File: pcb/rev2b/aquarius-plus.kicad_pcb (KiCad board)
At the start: 2 copper layers, 167 x 115 mm, 170 parts, among them J1 Power in, J10 FPGA spare, J11 Hand controller 2, J12 Hand controller 1, J13 ESP32 spare, J2 ESP USB Host, J3 Audio out, J4 VGA, J5 Cassette out, J6 Cassette in, J7 Expansion port, J8 Printer, J9 TF-03A, Q1 BC847C, Q2 BC847C, Q3 2N7002, SW1 SW_DPDT_x2, U1 SN74AHCT1G125DBVR, U10 ESP32-S3-WROOM-1-N4R2, U11 LDL1117S33R, U12 SN74CB3T3245PWR, U13 IS61C5128AS-25QLI, U2 SN74AHCT1G125DBVR, U3 LD1117S12, U4 SN74CB3T3245PWR, U5 MAX3221ECPWR, U6 XC6SLX9-2TQG144C, U7 Z84C0010AEG, U8 SN74CB3T3245PWR, U9 SN74CB3T3245PWR, X1 SX3M14.31818M20F30TNN

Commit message: Tweaks
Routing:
- net GND: track 884.0 -> 856.1 mm
- net MREQ#: track 99.7 -> 90.9 mm
- net +3V3: track 540.0 -> 537.5 mm
- net A7: track 135.6 -> 136.8 mm
- net D1: track 108.3 -> 107.7 mm
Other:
- board text added: "rev2b"
- board text removed: "rev2"

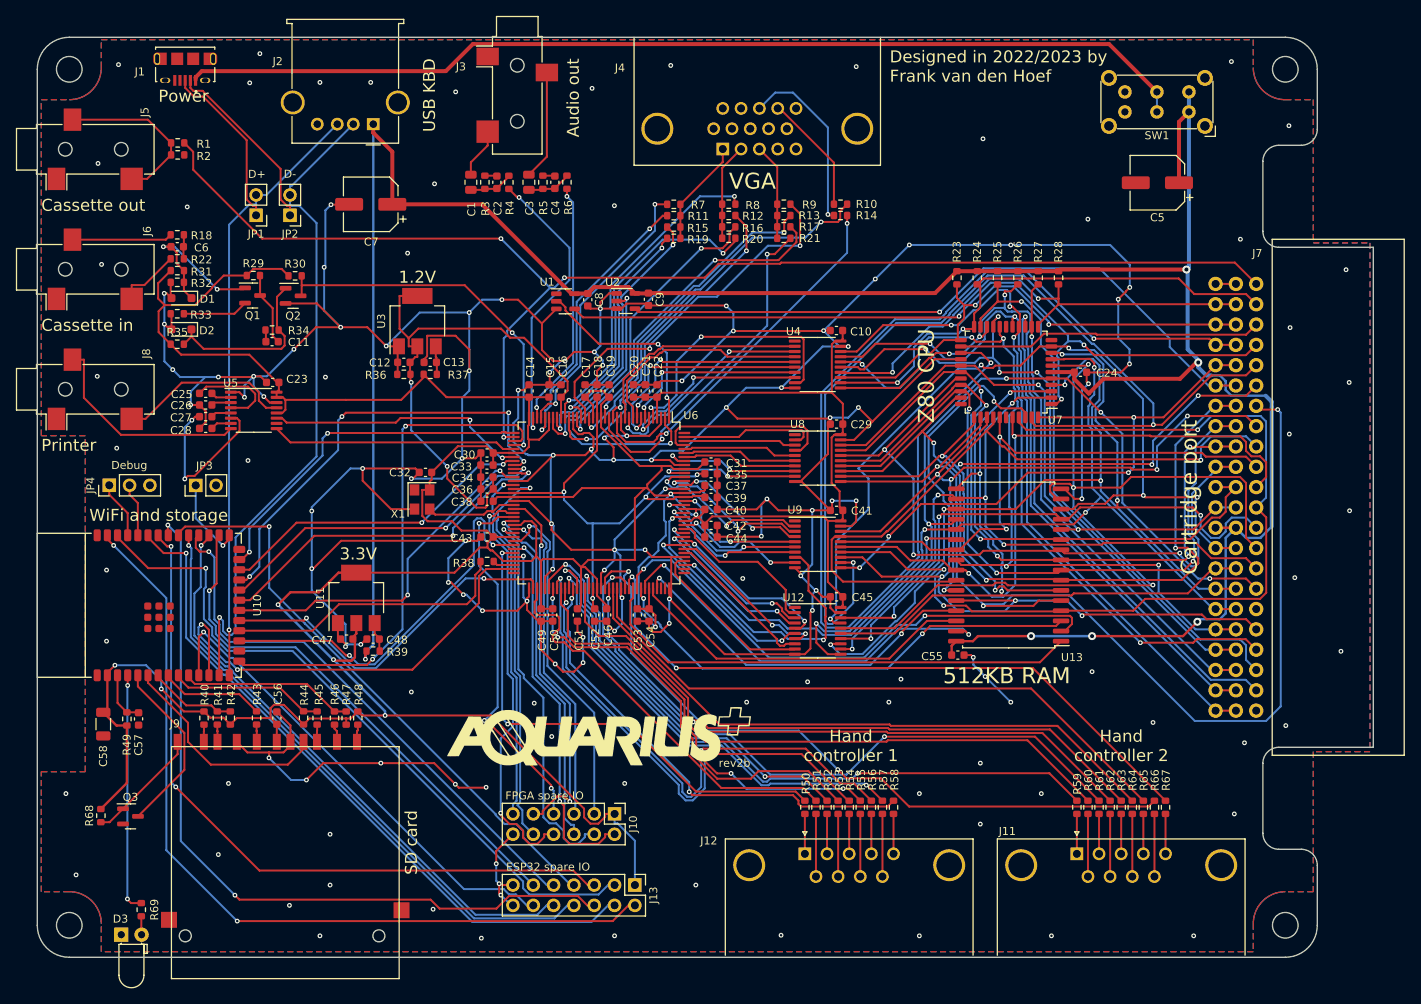
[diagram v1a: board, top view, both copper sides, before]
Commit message: Tweak traces and GND pins on PCB rev2b
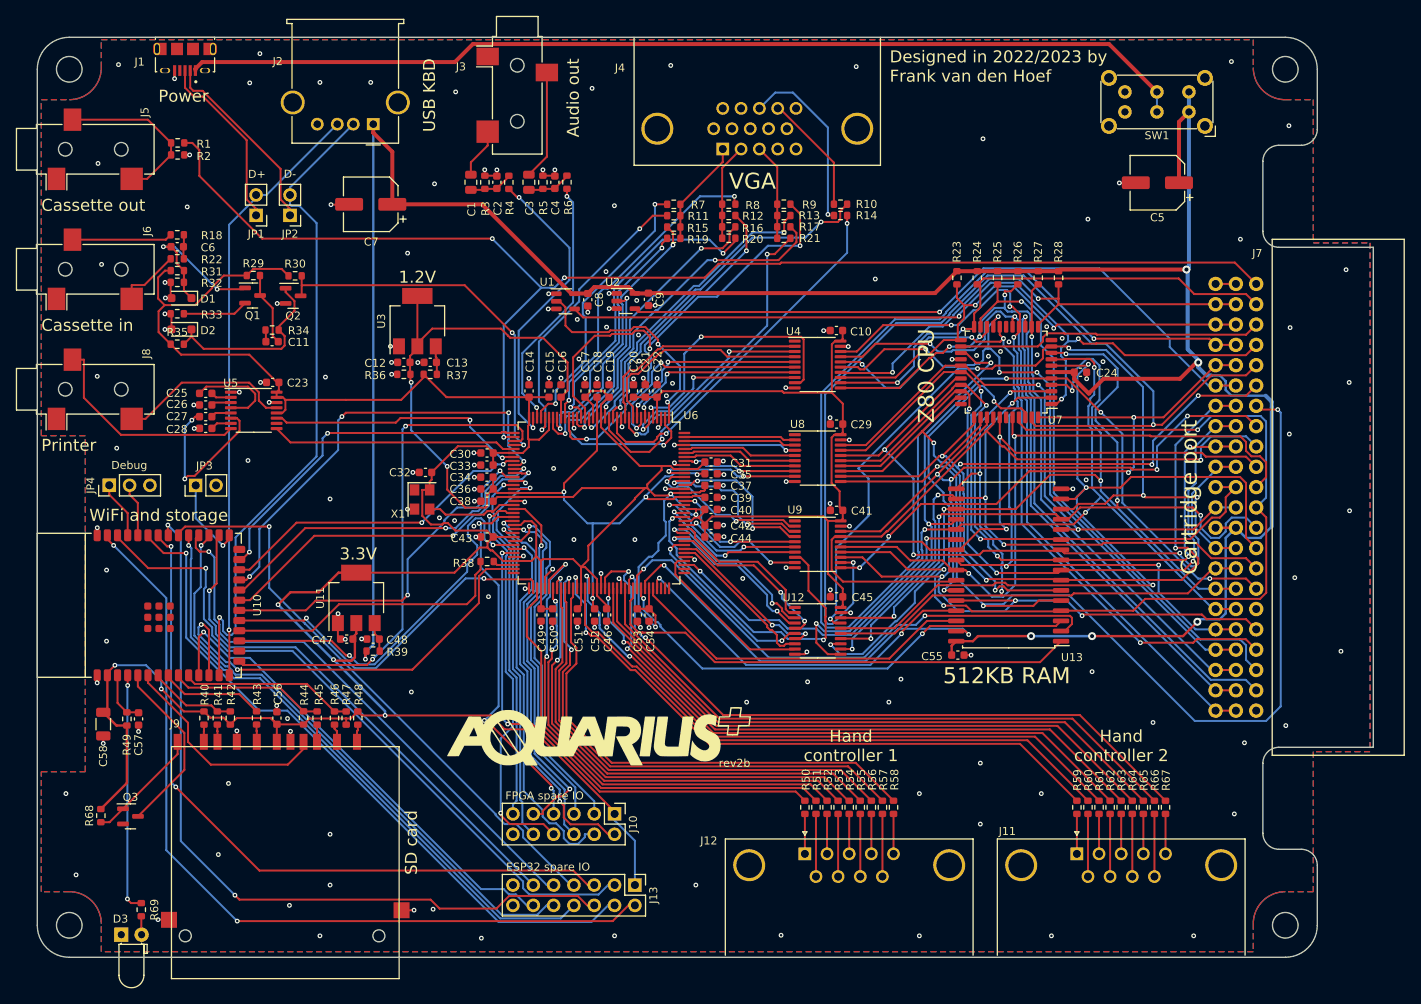
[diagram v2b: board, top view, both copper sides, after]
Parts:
- moved J1 1.23 mm to (83.5, 36.5)
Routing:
- net GND: track 856.1 -> 111.0 mm, vias 158 -> 195
- net HC1_D07: track 52.5 -> 68.5 mm
- net HC2_D03: track 88.7 -> 79.8 mm, vias 2 -> 0
- net HC1_D03: track 55.6 -> 64.3 mm
- net +3V3: track 537.5 -> 530.8 mm
- net HC1_D00: track 50.8 -> 56.8 mm
- net FPGA_A2: track 23.1 -> 18.2 mm, vias 0 -> 2
- net HC1_D02: track 54.4 -> 59.3 mm, vias 2 -> 0
- net HC2_D07: track 85.0 -> 80.2 mm
- net VGA_B3: track 46.2 -> 51.0 mm
- net HC2_D08: track 83.5 -> 79.0 mm
- net HC1_D01: track 53.7 -> 57.9 mm
- net FPGA_A6: track 17.8 -> 14.4 mm
- net HC1_D04: track 58.9 -> 62.2 mm, vias 2 -> 0
- net HC1_D05: track 63.5 -> 60.1 mm, vias 2 -> 0
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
